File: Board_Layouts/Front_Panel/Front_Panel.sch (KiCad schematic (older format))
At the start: 95 parts, among them J1 Conn_02x18_Odd_Even, SW1 SW_Push_SPDT, SW2 SW_Push, SW3 SW_Push, SW4 SW_SPDT, U1 74LS04, U10 74LS04, U2 74LS04, U3 74LS04, U4 7400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

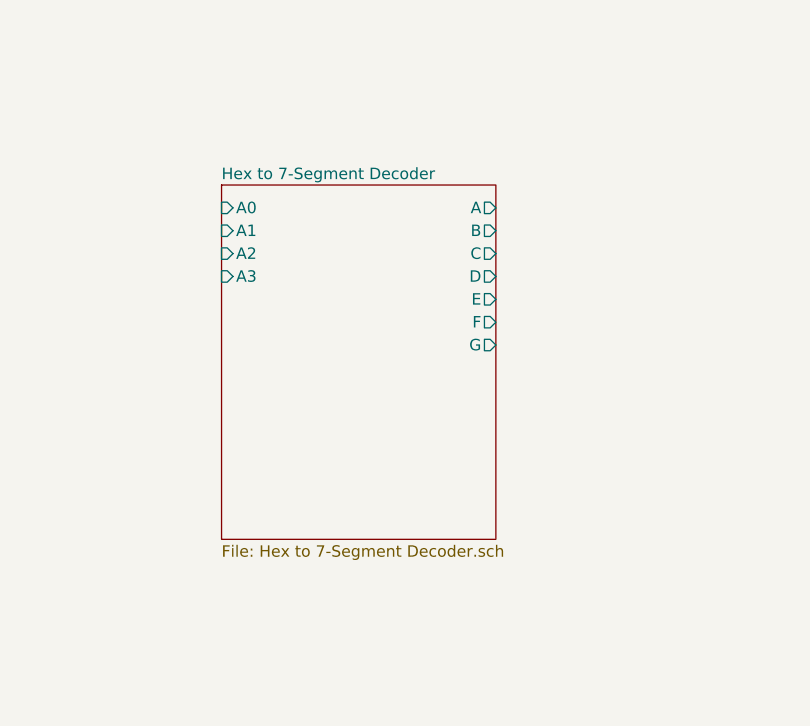
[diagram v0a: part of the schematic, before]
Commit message: Writing documentation renamed a bunch of stuff
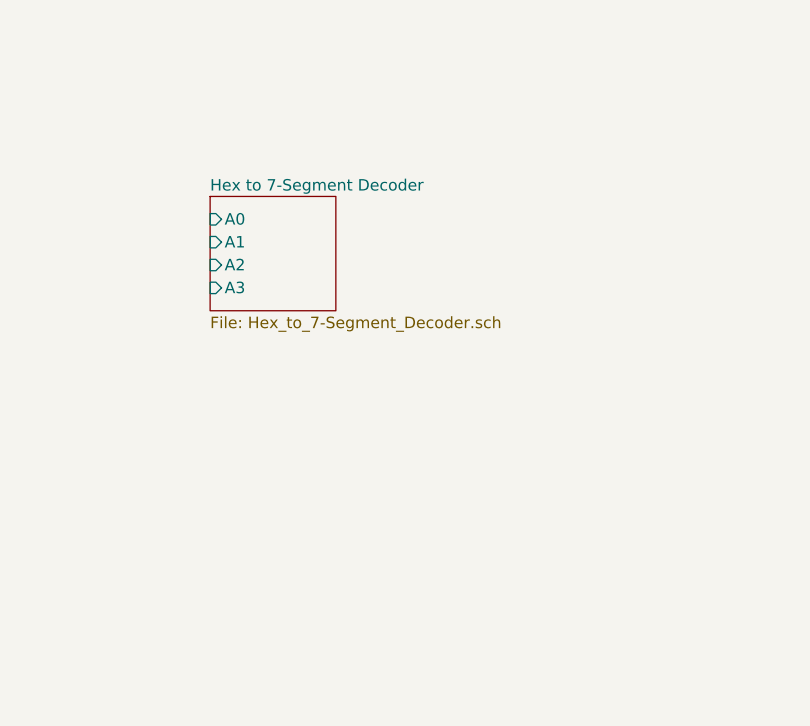
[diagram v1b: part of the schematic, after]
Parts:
- U1, U10, U2, U3, U4, U5, U6, U7, U8, U9: footprint Package_DIP:DIP-14_W7.62mm_Socket -> Package_DIP:DIP-14_W7.62mm

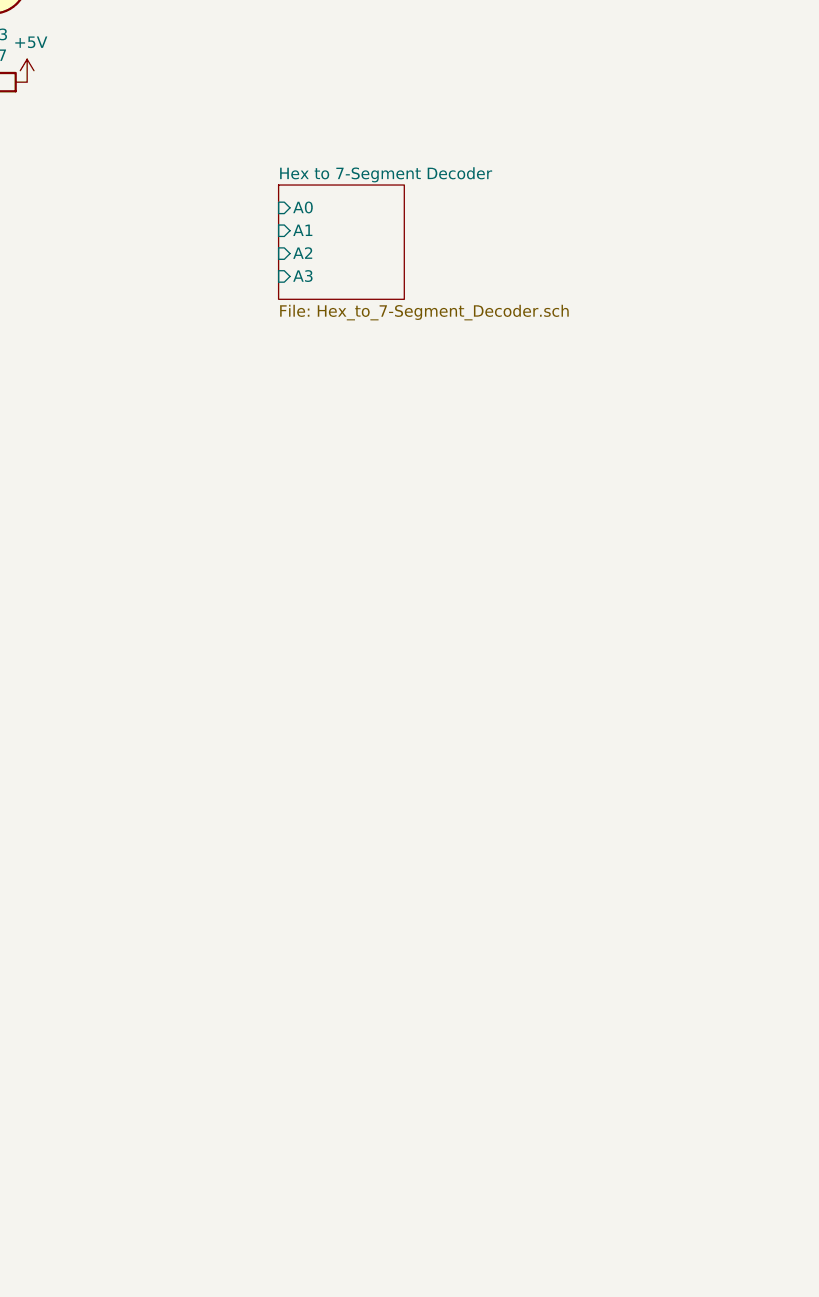
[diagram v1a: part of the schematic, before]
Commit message: Added hex decoders to front panel
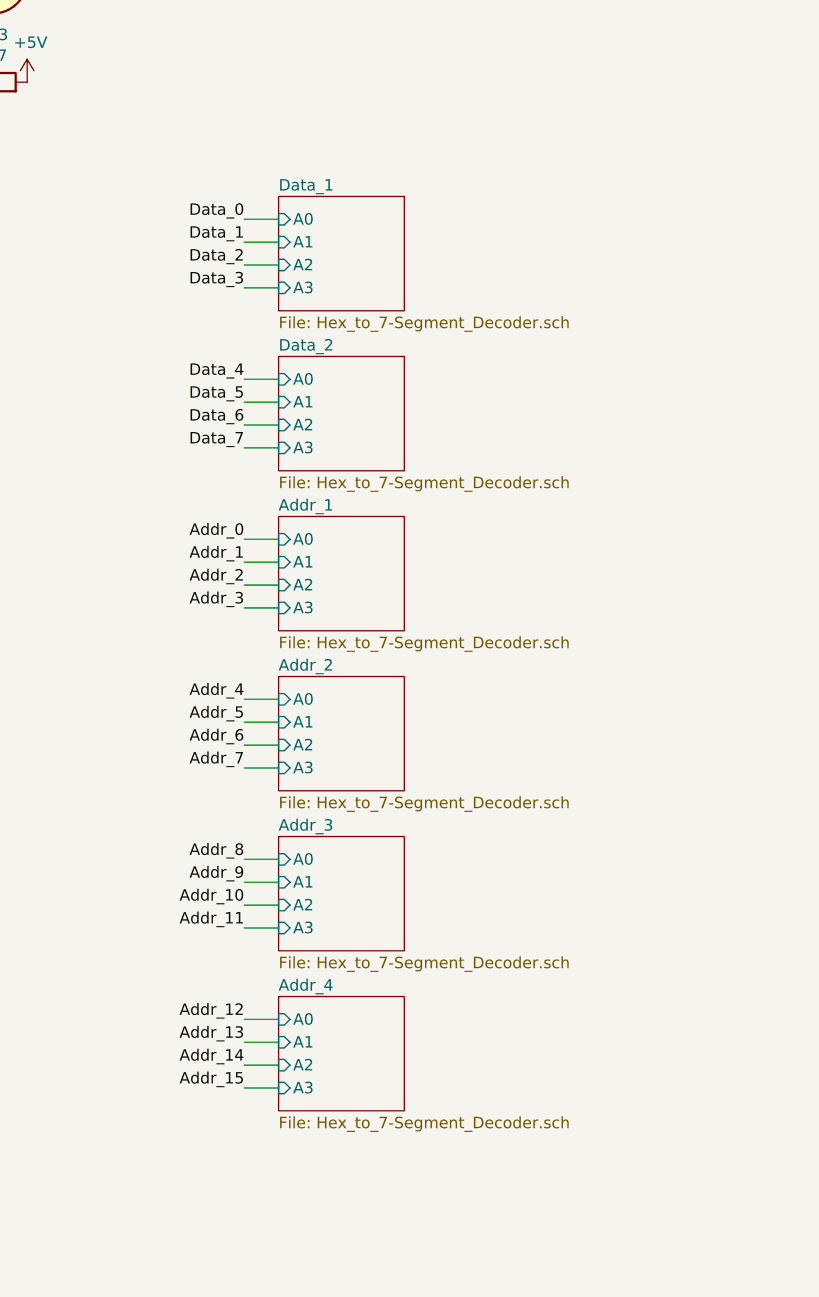
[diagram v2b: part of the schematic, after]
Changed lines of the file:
@@
 EESchema Schematic File Version 4
-LIBS:Front Panel-cache
+LIBS:Front_Panel-cache
 EELAYER 29 0
 EELAYER END
 $Descr A3 16535 11693
 encoding utf-8
-Sheet 1 2
+Sheet 1 7
 Title "Front Panel"
 Date "2019-03-23"
@@
 $EndComp
 $Sheet
-S 6750 4850 550  500
+S 6750 5600 550  500
 U 5C99B4A2
-F0 "Hex to 7-Segment Decoder" 50
+F0 "Data_2" 50
 F1 "Hex_to_7-Segment_Decoder.sch" 50
-F2 "A0" I L 6750 4950 50
-F3 "A1" I L 6750 5050 50
-F4 "A2" I L 6750 5150 50
-F5 "A3" I L 6750 5250 50
+F2 "A0" I L 6750 5700 50
+F3 "A1" I L 6750 5800 50
+F4 "A2" I L 6750 5900 50
+F5 "A3" I L 6750 6000 50
 $EndSheet
+$Sheet
+S 6750 4900 550  500
+U 5CAB8BF2
+F0 "Data_1" 50
+F1 "Hex_to_7-Segment_Decoder.sch" 50
+F2 "A0" I L 6750 5000 50
+F3 "A1" I L 6750 5100 50
+F4 "A2" I L 6750 5200 50
+F5 "A3" I L 6750 5300 50
+$EndSheet
+$Sheet
+S 6750 8400 550  500
+U 5CABA873
+F0 "Addr_4" 50
+F1 "Hex_to_7-Segment_Decoder.sch" 50
+F2 "A0" I L 6750 8500 50
+F3 "A1" I L 6750 8600 50
+F4 "A2" I L 6750 8700 50
+F5 "A3" I L 6750 8800 50
+$EndSheet
+$Sheet
+S 6750 7700 550  500
+U 5CABC1E4
+F0 "Addr_3" 50
+F1 "Hex_to_7-Segment_Decoder.sch" 50
+F2 "A0" I L 6750 7800 50
+F3 "A1" I L 6750 7900 50
+F4 "A2" I L 6750 8000 50
+F5 "A3" I L 6750 8100 50
+$EndSheet
+$Sheet
+S 6750 7000 550  500
+U 5CABDB41
+F0 "Addr_2" 50
+F1 "Hex_to_7-Segment_Decoder.sch" 50
+F2 "A0" I L 6750 7100 50
+F3 "A1" I L 6750 7200 50
+F4 "A2" I L 6750 7300 50
+F5 "A3" I L 6750 7400 50
+$EndSheet
+$Sheet
+S 6750 6300 550  500
+U 5CABF552
+F0 "Addr_1" 50
+F1 "Hex_to_7-Segment_Decoder.sch" 50
+F2 "A0" I L 6750 6400 50
+F3 "A1" I L 6750 6500 50
+F4 "A2" I L 6750 6600 50
+F5 "A3" I L 6750 6700 50
+$EndSheet
+Text Label 6600 5000 2    50   ~ 0
+Data_0
+Text Label 6600 5100 2    50   ~ 0
+Data_1
+Text Label 6600 5200 2    50   ~ 0
+Data_2
+Text Label 6600 5300 2    50   ~ 0
+Data_3
+Text Label 6600 5700 2    50   ~ 0
+Data_4
+Text Label 6600 5800 2    50   ~ 0
+Data_5
+Text Label 6600 5900 2    50   ~ 0
+Data_6
+Text Label 6600 6000 2    50   ~ 0
+Data_7
+Wire Wire Line
+	6750 5000 6600 5000
+Wire Wire Line
+	6750 5100 6600 5100
+Wire Wire Line
+	6750 5200 6600 5200
+Wire Wire Line
+	6750 5300 6600 5300
+Wire Wire Line
+	6750 5700 6600 5700
+Wire Wire Line
+	6750 5800 6600 5800
+Wire Wire Line
+	6750 5900 6600 5900
+Wire Wire Line
+	6750 6000 6600 6000
+Wire Wire Line
+	6750 6400 6600 6400
+Wire Wire Line
+	6750 6500 6600 6500
+Wire Wire Line
+	6750 6600 6600 6600
+Wire Wire Line
+	6750 6700 6600 6700
+Wire Wire Line
+	6750 7100 6600 7100
+Wire Wire Line
+	6750 7200 6600 7200
+Wire Wire Line
+	6750 7300 6600 7300
+Wire Wire Line
+	6750 7400 6600 7400
+Wire Wire Line
+	6750 7800 6600 7800
+Wire Wire Line
+	6750 7900 6600 7900
+Wire Wire Line
+	6750 8000 6600 8000
+Wire Wire Line
+	6750 8100 6600 8100
+Wire Wire Line
+	6750 8500 6600 8500
+Wire Wire Line
+	6750 8600 6600 8600
+Wire Wire Line
+	6750 8700 6600 8700
+Wire Wire Line
+	6750 8800 6600 8800
+Text Label 6600 6500 2    50   ~ 0
+Addr_1
+Text Label 6600 6600 2    50   ~ 0
+Addr_2
+Text Label 6600 6700 2    50   ~ 0
+Addr_3
+Text Label 6600 7100 2    50   ~ 0
+Addr_4
+Text Label 6600 7200 2    50   ~ 0
+Addr_5
+Text Label 6600 7300 2    50   ~ 0
+Addr_6
+Text Label 6600 7400 2    50   ~ 0
+Addr_7
+Text Label 6600 7800 2    50   ~ 0
+Addr_8
+Text Label 6600 7900 2    50   ~ 0
+Addr_9
+Text Label 6600 8000 2    50   ~ 0
+Addr_10
+Text Label 6600 8100 2    50   ~ 0
+Addr_11
+Text Label 6600 8500 2    50   ~ 0
+Addr_12
+Text Label 6600 8600 2    50   ~ 0
+Addr_13
+Text Label 6600 8700 2    50   ~ 0
+Addr_14
+Text Label 6600 8800 2    50   ~ 0
+Addr_15
+Text Label 6600 6400 2    50   ~ 0
+Addr_0
 $EndSCHEMATC
